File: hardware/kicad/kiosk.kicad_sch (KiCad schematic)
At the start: 16 parts, among them J10 Jack 5V rail 1, J11 Jack 5V rail 2, J12 Mo rong: P2,P4..P7 dua ra, J13 PCF8574: han day tu hang P sa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, J3 LCD 4.0in ST7796S + GT911, J4 VL53L1X, J5 PCF8574 0x20 - de cam hang I2C, J6 DS3231, J7 MAX98357A, J9 SG90 servo, U1 ESP32-S3-CAM N16R8

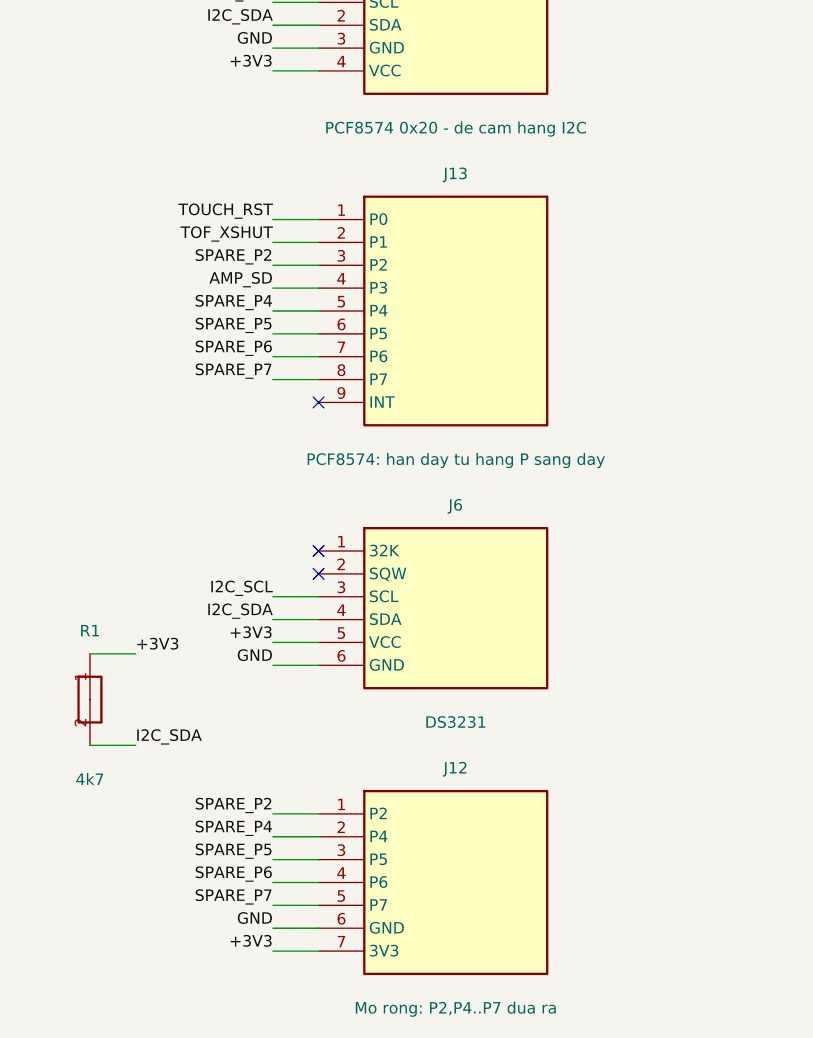
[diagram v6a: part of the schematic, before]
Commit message: refactor(hardware): drop J12 and the six spare holes it fed
J12 brought the expander's unused port pins out to a header. That made
sense while J13 was a socket underneath the module, where those pins were
buried. It stopped making sense the moment the port row became soldered
wire: a wire can be soldered wherever it is wanted, so a landing pad on
this board buys nothing.

The same argument empties six of J13's nine holes, so J13 becomes the
three the firmware actually drives - P0, P1, P3 - and the SPARE nets go
with it.

Section 2.4 still names the expander as the only room to grow, and now
says where that room is: the module's own port row, which stays exposed,
not a connector on this board.

Fifteen parts, twenty-two nets.
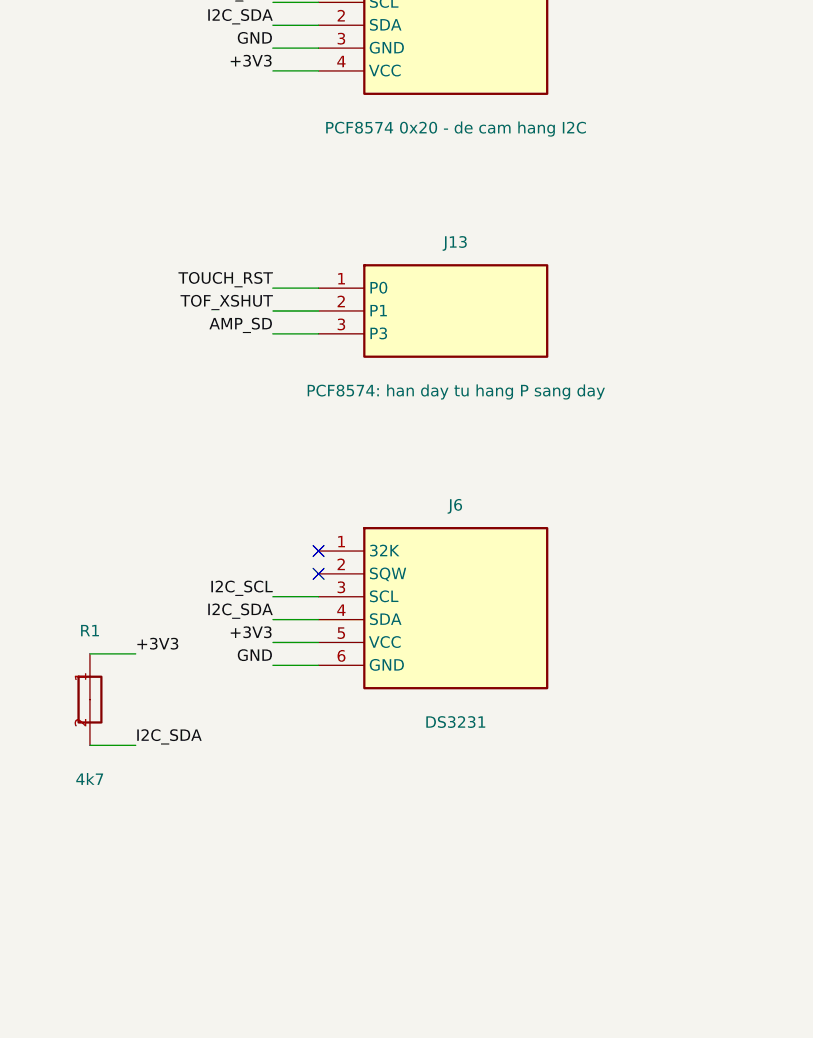
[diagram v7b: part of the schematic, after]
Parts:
- removed J12: Mo rong: P2,P4..P7 dua ra, Connector_PinHeader_2.54mm:PinHeader_1x07_P2.54mm_Vertical, symbol kiosk:J12
- J13: footprint Connector_PinHeader_2.54mm:PinHeader_1x09_P2.54mm_Vertical -> Connector_PinHeader_2.54mm:PinHeader_1x03_P2.54mm_Vertical
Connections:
- net SPARE_P2 is gone; now on net AMP_SD: J13.3 (P3)
- net AMP_SD: no longer J13.4 (P3)
- removed net SPARE_P4: J13.5 (P4)
- removed net SPARE_P5: J13.6 (P5)
- removed net SPARE_P6: J13.7 (P6)
- removed net SPARE_P7: J13.8 (P7)
- no-connect marks 27 -> 26

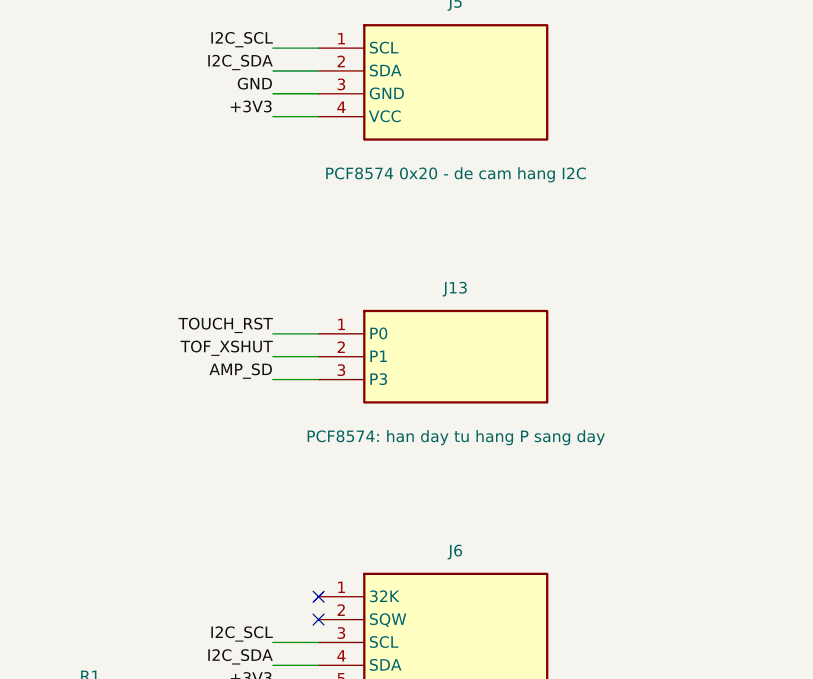
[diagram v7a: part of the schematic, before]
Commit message: fix(hardware): seat the expander on its port row and free the RTC's area
Three corrections, all from looking at the parts rather than at my model
of them.

The expander seats on the nine-pin row down its long edge, not on the
four-pin row across the short one. Nine pins over 48 mm hold it; four
over 16 mm leave it cantilevered on a board that carries a servo. So J13
becomes the socket and J5 the four holes that take wires from the bus row
standing up above it. The six port pins carrying no signal still need
holes - that is what the module stands on.

The RTC does not lie on the board at all; it plugs in standing. It needed
six holes, not the 19 by 42 mm rectangle reserved for it, and that space
goes back.

Three module outlines left where there were five, and the panel's is
confirmed right.
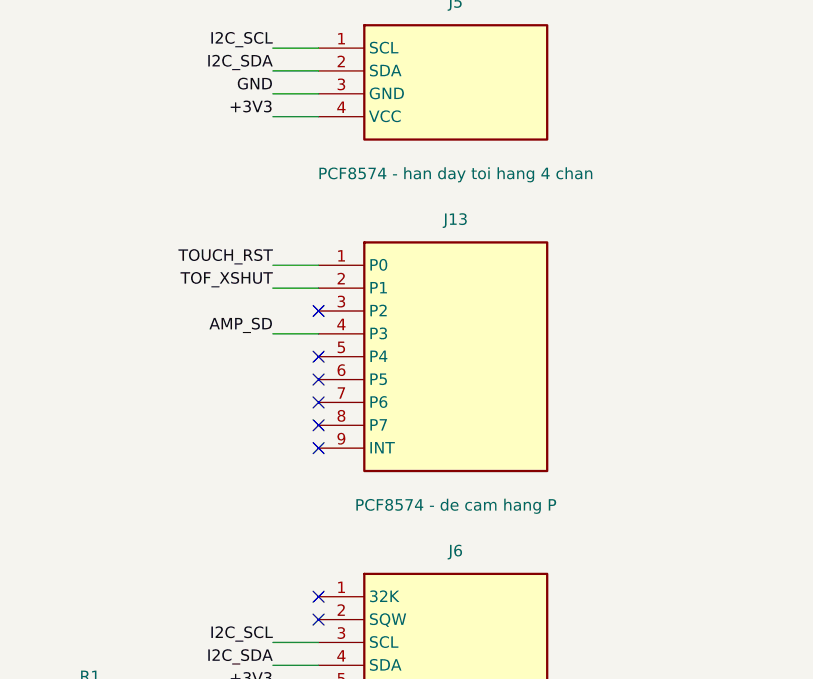
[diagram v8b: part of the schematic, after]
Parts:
- J13: value PCF8574: han day tu hang P sang day -> PCF8574 - de cam hang P; footprint Connector_PinHeader_2.54mm:PinHeader_1x03_P2.54mm_Vertical -> Connector_PinSocket_2.54mm:PinSocket_1x09_P2.54mm_Vertical
- J5: value PCF8574 0x20 - de cam hang I2C -> PCF8574 - han day toi hang 4 chan; footprint Connector_PinSocket_2.54mm:PinSocket_1x04_P2.54mm_Vertical -> Connector_PinHeader_2.54mm:PinHeader_1x04_P2.54mm_Vertical
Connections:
- net AMP_SD: now also J13.4 (P3); no longer J13.3 (P3)
- no-connect marks 26 -> 32
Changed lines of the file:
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@@
     (exclude_from_sim no) (in_bom yes) (on_board yes) (dnp no)
     (property "Reference" "J5" (at 190.5 133.35 0) (effects (font (size 1.27 1.27))))
-    (property "Value" "PCF8574 0x20 - de cam hang I2C" (at 190.5 152.4 0) (effects (font (size 1.27 1.27))))
-    (property "Footprint" "Connector_PinSocket_2.54mm:PinSocket_1x04_P2.54mm_Vertical" (at 190.5 142.24 0)
+    (property "Value" "PCF8574 - han day toi hang 4 chan" (at 190.5 152.4 0) (effects (font (size 1.27 1.27))))
+    (property "Footprint" "Connector_PinHeader_2.54mm:PinHeader_1x04_P2.54mm_Vertical" (at 190.5 142.24 0)
       (effects (font (size 1.27 1.27)) hide))
     (property "Datasheet" "" (at 190.5 142.24 0) (effects (font (size 1.27 1.27)) hide))
@@
   (symbol (lib_id "kiosk:J13") (at 190.5 172.72 0) (unit 1)
     (exclude_from_sim no) (in_bom yes) (on_board yes) (dnp no)
-    (property "Reference" "J13" (at 190.5 165.1 0) (effects (font (size 1.27 1.27))))
-    (property "Value" "PCF8574: han day tu hang P sang day" (at 190.5 181.60999999999999 0) (effects (font (size 1.27 1.27))))
-    (property "Footprint" "Connector_PinHeader_2.54mm:PinHeader_1x03_P2.54mm_Vertical" (at 190.5 172.72 0)
+    (property "Reference" "J13" (at 190.5 157.48 0) (effects (font (size 1.27 1.27))))
+    (property "Value" "PCF8574 - de cam hang P" (at 190.5 189.23 0) (effects (font (size 1.27 1.27))))
+    (property "Footprint" "Connector_PinSocket_2.54mm:PinSocket_1x09_P2.54mm_Vertical" (at 190.5 172.72 0)
       (effects (font (size 1.27 1.27)) hide))
     (property "Datasheet" "" (at 190.5 172.72 0) (effects (font (size 1.27 1.27)) hide))
@@
     (pin "2")
     (pin "3")
+    (pin "4")
+    (pin "5")
+    (pin "6")
+    (pin "7")
+    (pin "8")
+    (pin "9")
     (instances
       (project "kiosk"
@@
     )
   )
+  (wire (pts (xy 175.26 162.56) (xy 170.17999999999998 162.56))
+    (stroke (width 0) (type default)))
+  (label "TOUCH_RST" (at 170.17999999999998 162.56 180)
+    (effects (font (size 1.27 1.27)) (justify right bottom))
+)
+  (wire (pts (xy 175.26 165.1) (xy 170.17999999999998 165.1))
+    (stroke (width 0) (type default)))
+  (label "TOF_XSHUT" (at 170.17999999999998 165.1 180)
+    (effects (font (size 1.27 1.27)) (justify right bottom))
+)
+  (no_connect (at 175.26 167.64000000000001))
   (wire (pts (xy 175.26 170.18) (xy 170.17999999999998 170.18))
     (stroke (width 0) (type default)))
-  (label "TOUCH_RST" (at 170.17999999999998 170.18 180)
+  (label "AMP_SD" (at 170.17999999999998 170.18 180)
     (effects (font (size 1.27 1.27)) (justify right bottom))
 )
-  (wire (pts (xy 175.26 172.72) (xy 170.17999999999998 172.72))
-    (stroke (width 0) (type default)))
-  (label "TOF_XSHUT" (at 170.17999999999998 172.72 180)
-    (effects (font (size 1.27 1.27)) (justify right bottom))
-)
-  (wire (pts (xy 175.26 175.26000000000002) (xy 170.17999999999998 175.26000000000002))
-    (stroke (width 0) (type default)))
-  (label "AMP_SD" (at 170.17999999999998 175.26000000000002 180)
-    (effects (font (size 1.27 1.27)) (justify right bottom))
-)
+  (no_connect (at 175.26 172.72))
+  (no_connect (at 175.26 175.26))
+  (no_connect (at 175.26 177.8))
+  (no_connect (at 175.26 180.34))
+  (no_connect (at 175.26 182.88))
   (symbol (lib_id "kiosk:J6") (at 190.5 205.74 0) (unit 1)
     (exclude_from_sim no) (in_bom yes) (on_board yes) (dnp no)
